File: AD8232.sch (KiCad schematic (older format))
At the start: 33 parts

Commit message: conectar simbolos en el esquematico
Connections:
- net GND: now reaches JP?.1 (A)
- net GND: now also C?.1, C?.1, J?.1 (Pin_1), M?.16 (GND), M?.PAD (GND_PAD), R?.1, R?.2
- net at JP?.2 (B): now also D?.1 (K)
- net RL: now reaches J?.1 (Pin_1)
- net RL: now also J?.T, R?.2
- net LA: now reaches J?.2 (Pin_2)
- net LA: now also J?.R, R?.2, R?.2
- net RA: now reaches J?.3 (Pin_3)
- net RA: now also J?.S, R?.2, R?.2
- net at D?.2 (A): now also R?.2
- net +3V3: now reaches J?.2 (Pin_2)
- net +3V3: now also C?.2, M?.15 (FR), M?.17 (+VS), R?.1, R?.1, R?.2, R?.2
- net SIGNAL_OUT: now reaches J?.3 (Pin_3)
- net SIGNAL_OUT: now also C?.2, M?.10 (OUT), R?.1, R?.2
- net LO-: now reaches J?.4 (Pin_4)
- net LO-: now also M?.11 (LO-)
- net LO+: now reaches J?.5 (Pin_5)
- net LO+: now also M?.12 (LO+)
- net SDN: now reaches J?.6 (Pin_6)
- net SDN: now also M?.13 (~SDN), R?.2
- net at M?.1 (HPDRIVE): now also C?.2
- net at M?.14 (AC/~DC): now also R?.1, R?.2
- net at M?.18 (REFIN): now also C?.2, R?.1, R?.2
- net at M?.19 (IAOUT): now also R?.1, R?.1
- net at M?.2 (+IN): now also R?.1
- net at M?.20 (HPSENSE): now also C?.1, R?.2
- net at M?.3 (-IN): now also R?.1
- net at M?.4 (RLDFB): now also C?.1
- net at M?.5 (RLD): now also C?.2, R?.1
- net at M?.6 (SW): now also C?.2, R?.1, R?.2
- net at M?.7 (OPAMP+): now also C?.1, R?.1
- net REFOUT: now reaches M?.8 (REFOUT)
- net REFOUT: now also C?.1, C?.2, R?.1
- net at M?.9 (OPAMP-): now also R?.1, R?.2
- net at R?.1: now also R?.1, R?.1, R?.2
- net at R?.2: now also C?.1, R?.2
- net at R?.1: now also R?.1, R?.2
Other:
- moved on the sheet: C?, D?, J?, JP?, M?, R?

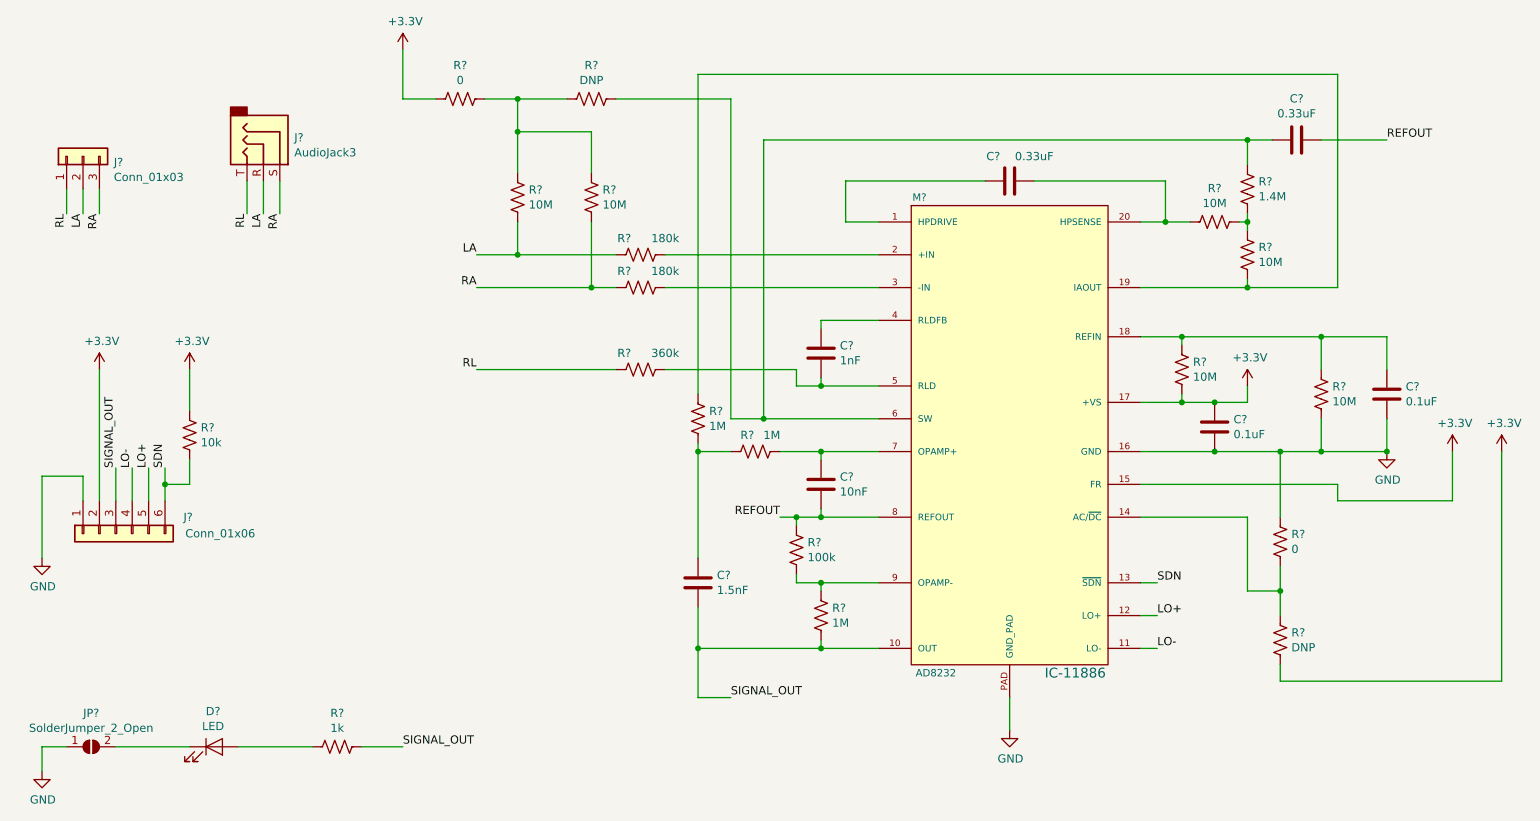
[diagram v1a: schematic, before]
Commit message: anotar simbolos del esquema
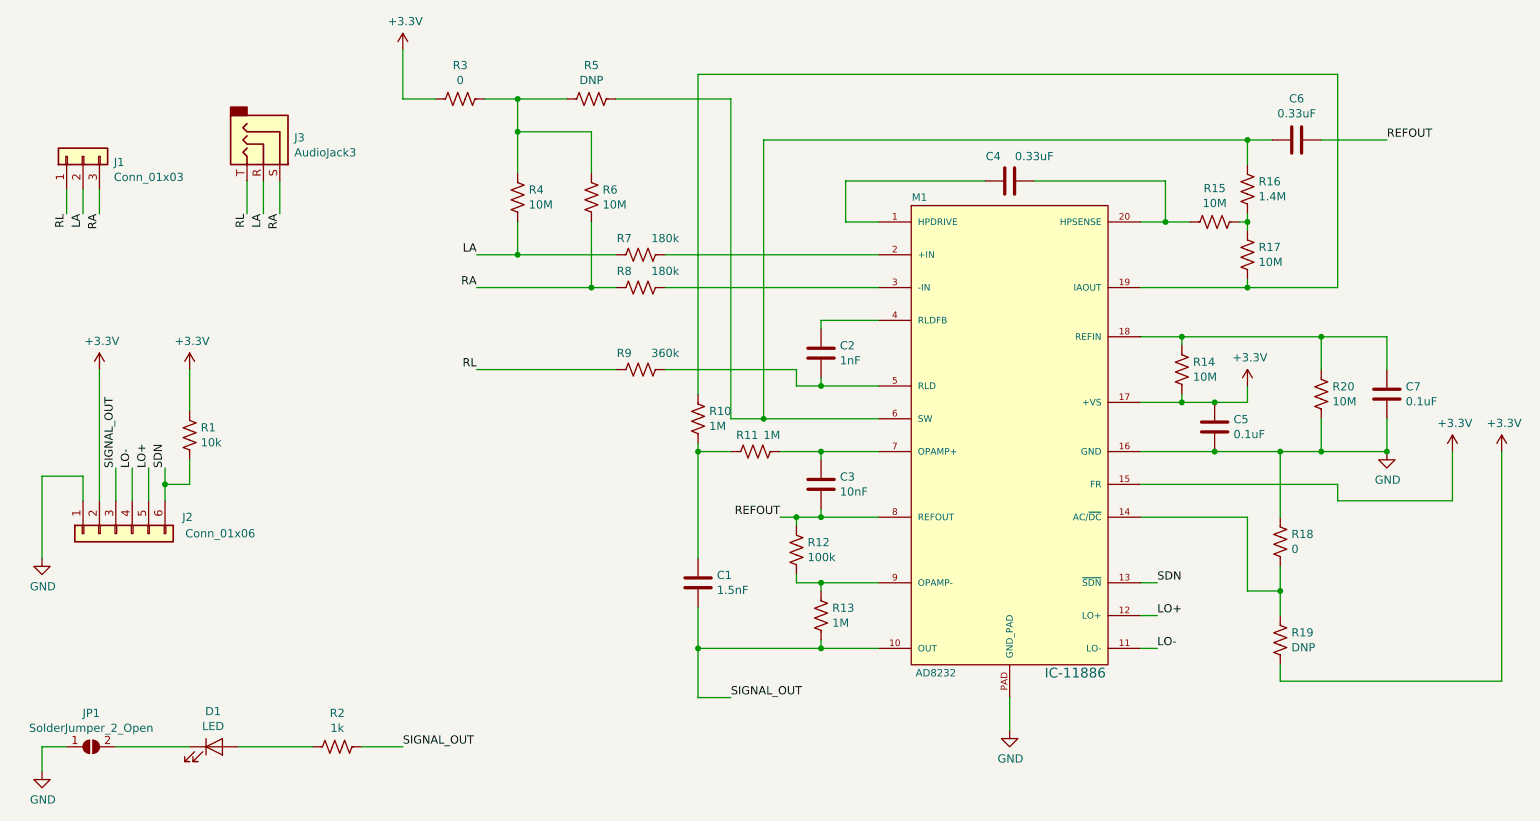
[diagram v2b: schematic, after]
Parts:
- gave numbers to parts that had none: 33

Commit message: agregar huellas a los simbolos en el esquematico
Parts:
- C1, C2, C3, C5, C7: footprint (none) -> Capacitor_SMD:C_0603_1608Metric
- C4, C6: footprint (none) -> Capacitor_SMD:C_0805_2012Metric
- D1: footprint (none) -> LED_SMD:LED_0603_1608Metric
- J1: footprint (none) -> Connector_Wire:SolderWirePad_1x03_P7.62mm_Drill2.5mm
- J2: footprint (none) -> TerminalBlock_TE-Connectivity:TerminalBlock_TE_282834-6_1x06_P2.54mm_Horizontal
- J3: footprint (none) -> Connector_Audio:Jack_3.5mm_CUI_SJ-3523-SMT_Horizontal
- JP1: footprint (none) -> Jumper:SolderJumper-2_P1.3mm_Open_RoundedPad1.0x1.5mm
- M1: footprint LFCSP_20 -> Package_CSP:LFCSP-20-1EP_4x4mm_P0.5mm_EP2.5x2.5mm
- R1, R10, R11, R12, R13, R14, R15, R16, R17, R18, R19, R2, R20, R3, R4, R5, R6, R7, R8, R9: footprint (none) -> Resistor_SMD:R_0603_1608Metric
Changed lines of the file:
@@
 F 0 "J1" V 1664 2212 50  0000 R CNN
 F 1 "Conn_01x03" V 1573 2212 50  0000 R CNN
-F 2 "" H 1700 2400 50  0001 C CNN
+F 2 "Connector_Wire:SolderWirePad_1x03_P7.62mm_Drill2.5mm" H 1700 2400 50  0001 C CNN
 F 3 "~" H 1700 2400 50  0001 C CNN
 	1    1700 2400
@@
 F 0 "J3" V 2736 2538 50  0000 L CNN
 F 1 "AudioJack3" V 2827 2538 50  0000 L CNN
-F 2 "" H 2800 2350 50  0001 C CNN
+F 2 "Connector_Audio:Jack_3.5mm_CUI_SJ-3523-SMT_Horizontal" H 2800 2350 50  0001 C CNN
 F 3 "~" H 2800 2350 50  0001 C CNN
 	1    2800 2350
@@
 F 0 "JP1" H 1750 6205 50  0000 C CNN
 F 1 "SolderJumper_2_Open" H 1750 6114 50  0000 C CNN
-F 2 "" H 1750 6000 50  0001 C CNN
+F 2 "Jumper:SolderJumper-2_P1.3mm_Open_RoundedPad1.0x1.5mm" H 1750 6000 50  0001 C CNN
 F 3 "~" H 1750 6000 50  0001 C CNN
 	1    1750 6000
@@
 F 0 "D1" H 2493 6216 50  0000 C CNN
 F 1 "LED" H 2493 6125 50  0000 C CNN
-F 2 "" H 2500 6000 50  0001 C CNN
+F 2 "LED_SMD:LED_0603_1608Metric" H 2500 6000 50  0001 C CNN
 F 3 "~" H 2500 6000 50  0001 C CNN
 	1    2500 6000
@@
 F 0 "R4" H 4418 2696 50  0000 L CNN
 F 1 "10M" H 4418 2605 50  0000 L CNN
-F 2 "" V 4390 2640 50  0001 C CNN
+F 2 "Resistor_SMD:R_0603_1608Metric" V 4390 2640 50  0001 C CNN
 F 3 "~" H 4350 2650 50  0001 C CNN
 	1    4350 2650
@@
 F 0 "R6" H 4868 2696 50  0000 L CNN
 F 1 "10M" H 4868 2605 50  0000 L CNN
-F 2 "" V 4840 2640 50  0001 C CNN
+F 2 "Resistor_SMD:R_0603_1608Metric" V 4840 2640 50  0001 C CNN
 F 3 "~" H 4800 2650 50  0001 C CNN
 	1    4800 2650
@@
 F 0 "R7" V 5000 2900 50  0000 C CNN
 F 1 "180k" V 5000 3150 50  0000 C CNN
-F 2 "" V 5140 2990 50  0001 C CNN
+F 2 "Resistor_SMD:R_0603_1608Metric" V 5140 2990 50  0001 C CNN
 F 3 "~" H 5100 3000 50  0001 C CNN
 	1    5100 3000
@@
 F 0 "R8" V 5000 3100 50  0000 C CNN
 F 1 "180k" V 5000 3350 50  0000 C CNN
-F 2 "" V 5140 3190 50  0001 C CNN
+F 2 "Resistor_SMD:R_0603_1608Metric" V 5140 3190 50  0001 C CNN
 F 3 "~" H 5100 3200 50  0001 C CNN
 	1    5100 3200
@@
 F 0 "R9" V 5000 3600 50  0000 C CNN
 F 1 "360k" V 5000 3850 50  0000 C CNN
-F 2 "" V 5140 3690 50  0001 C CNN
+F 2 "Resistor_SMD:R_0603_1608Metric" V 5140 3690 50  0001 C CNN
 F 3 "~" H 5100 3700 50  0001 C CNN
 	1    5100 3700
@@
 F 0 "R10" H 5518 4046 50  0000 L CNN
 F 1 "1M" H 5518 3955 50  0000 L CNN
-F 2 "" V 5490 3990 50  0001 C CNN
+F 2 "Resistor_SMD:R_0603_1608Metric" V 5490 3990 50  0001 C CNN
 F 3 "~" H 5450 4000 50  0001 C CNN
 	1    5450 4000
@@
 F 0 "R11" V 5700 4150 50  0000 C CNN
 F 1 "1M" V 5700 4300 50  0000 C CNN
-F 2 "" V 5840 4190 50  0001 C CNN
+F 2 "Resistor_SMD:R_0603_1608Metric" V 5840 4190 50  0001 C CNN
 F 3 "~" H 5800 4200 50  0001 C CNN
 	1    5800 4200
@@
 F 0 "C1" H 5565 5046 50  0000 L CNN
 F 1 "1.5nF" H 5565 4955 50  0000 L CNN
-F 2 "" H 5488 4850 50  0001 C CNN
+F 2 "Capacitor_SMD:C_0603_1608Metric" H 5488 4850 50  0001 C CNN
 F 3 "~" H 5450 5000 50  0001 C CNN
 	1    5450 5000
@@
 F 0 "C2" H 6315 3646 50  0000 L CNN
 F 1 "1nF" H 6315 3555 50  0000 L CNN
-F 2 "" H 6238 3450 50  0001 C CNN
+F 2 "Capacitor_SMD:C_0603_1608Metric" H 6238 3450 50  0001 C CNN
 F 3 "~" H 6200 3600 50  0001 C CNN
 	1    6200 3600
@@
 F 0 "C3" H 6315 4446 50  0000 L CNN
 F 1 "10nF" H 6315 4355 50  0000 L CNN
-F 2 "" H 6238 4250 50  0001 C CNN
+F 2 "Capacitor_SMD:C_0603_1608Metric" H 6238 4250 50  0001 C CNN
 F 3 "~" H 6200 4400 50  0001 C CNN
 	1    6200 4400
@@
 F 0 "R12" H 6118 4846 50  0000 L CNN
 F 1 "100k" H 6118 4755 50  0000 L CNN
-F 2 "" V 6090 4790 50  0001 C CNN
+F 2 "Resistor_SMD:R_0603_1608Metric" V 6090 4790 50  0001 C CNN
 F 3 "~" H 6050 4800 50  0001 C CNN
 	1    6050 4800
@@
 F 0 "R13" H 6268 5246 50  0000 L CNN
 F 1 "1M" H 6268 5155 50  0000 L CNN
-F 2 "" V 6240 5190 50  0001 C CNN
+F 2 "Resistor_SMD:R_0603_1608Metric" V 6240 5190 50  0001 C CNN
 F 3 "~" H 6200 5200 50  0001 C CNN
 	1    6200 5200
@@
 F 0 "C4" V 7200 2450 50  0000 C CNN
 F 1 "0.33uF" V 7200 2700 50  0000 C CNN
-F 2 "" H 7388 2400 50  0001 C CNN
+F 2 "Capacitor_SMD:C_0805_2012Metric" H 7388 2400 50  0001 C CNN
 F 3 "~" H 7350 2550 50  0001 C CNN
 	1    7350 2550
@@
 F 0 "M1" H 6800 6150 45  0000 C CNN
 F 1 "AD8232" H 6900 3250 45  0000 C CNN
-F 2 "LFCSP_20" H 7350 6200 20  0001 C CNN
+F 2 "Package_CSP:LFCSP-20-1EP_4x4mm_P0.5mm_EP2.5x2.5mm" H 7350 6200 20  0001 C CNN
 F 3 "" H 7350 4400 60  0001 C CNN
 F 4 "IC-11886" H 7750 3250 60  0000 C CNN "Campo4"
@@
 F 0 "C5" H 8485 4004 50  0000 R CNN
 F 1 "0.1uF" H 8485 4095 50  0000 R CNN
-F 2 "" H 8638 3900 50  0001 C CNN
+F 2 "Capacitor_SMD:C_0603_1608Metric" H 8638 3900 50  0001 C CNN
 F 3 "~" H 8600 4050 50  0001 C CNN
 	1    8600 4050
@@
 F 0 "R14" H 8468 3746 50  0000 L CNN
 F 1 "10M" H 8468 3655 50  0000 L CNN
-F 2 "" V 8440 3690 50  0001 C CNN
+F 2 "Resistor_SMD:R_0603_1608Metric" V 8440 3690 50  0001 C CNN
 F 3 "~" H 8400 3700 50  0001 C CNN
 	1    8400 3700
@@
 F 0 "R15" V 8395 2800 50  0000 C CNN
 F 1 "10M" V 8486 2800 50  0000 C CNN
-F 2 "" V 8640 2790 50  0001 C CNN
+F 2 "Resistor_SMD:R_0603_1608Metric" V 8640 2790 50  0001 C CNN
 F 3 "~" H 8600 2800 50  0001 C CNN
 	1    8600 2800
@@
 F 0 "R16" H 8732 2554 50  0000 R CNN
 F 1 "1.4M" H 8732 2645 50  0000 R CNN
-F 2 "" V 8840 2590 50  0001 C CNN
+F 2 "Resistor_SMD:R_0603_1608Metric" V 8840 2590 50  0001 C CNN
 F 3 "~" H 8800 2600 50  0001 C CNN
 	1    8800 2600
@@
 F 0 "R17" H 8732 2954 50  0000 R CNN
 F 1 "10M" H 8732 3045 50  0000 R CNN
-F 2 "" V 8840 2990 50  0001 C CNN
+F 2 "Resistor_SMD:R_0603_1608Metric" V 8840 2990 50  0001 C CNN
 F 3 "~" H 8800 3000 50  0001 C CNN
 	1    8800 3000
@@
 F 0 "C6" V 8848 2300 50  0000 C CNN
 F 1 "0.33uF" V 8939 2300 50  0000 C CNN
-F 2 "" H 9138 2150 50  0001 C CNN
+F 2 "Capacitor_SMD:C_0805_2012Metric" H 9138 2150 50  0001 C CNN
 F 3 "~" H 9100 2300 50  0001 C CNN
 	1    9100 2300
@@
 F 0 "R20" H 9182 3804 50  0000 R CNN
 F 1 "10M" H 9182 3895 50  0000 R CNN
-F 2 "" V 9290 3840 50  0001 C CNN
+F 2 "Resistor_SMD:R_0603_1608Metric" V 9290 3840 50  0001 C CNN
 F 3 "~" H 9250 3850 50  0001 C CNN
 	1    9250 3850
@@
 F 0 "C7" H 9535 3804 50  0000 R CNN
 F 1 "0.1uF" H 9535 3895 50  0000 R CNN
-F 2 "" H 9688 3700 50  0001 C CNN
+F 2 "Capacitor_SMD:C_0603_1608Metric" H 9688 3700 50  0001 C CNN
 F 3 "~" H 9650 3850 50  0001 C CNN
 	1    9650 3850
@@
 F 0 "R1" H 2418 4146 50  0000 L CNN
 F 1 "10k" H 2418 4055 50  0000 L CNN
-F 2 "" V 2390 4090 50  0001 C CNN
+F 2 "Resistor_SMD:R_0603_1608Metric" V 2390 4090 50  0001 C CNN
 F 3 "~" H 2350 4100 50  0001 C CNN
 	1    2350 4100
@@
 F 0 "R2" V 3045 6000 50  0000 C CNN
 F 1 "1k" V 3136 6000 50  0000 C CNN
-F 2 "" V 3290 5990 50  0001 C CNN
+F 2 "Resistor_SMD:R_0603_1608Metric" V 3290 5990 50  0001 C CNN
 F 3 "~" H 3250 6000 50  0001 C CNN
 	1    3250 6000
@@
 F 0 "R3" V 3795 2050 50  0000 C CNN
 F 1 "0" V 3886 2050 50  0000 C CNN
-F 2 "" V 4040 2040 50  0001 C CNN
+F 2 "Resistor_SMD:R_0603_1608Metric" V 4040 2040 50  0001 C CNN
 F 3 "~" H 4000 2050 50  0001 C CNN
 	1    4000 2050
@@
 F 0 "R5" V 4595 2050 50  0000 C CNN
 F 1 "DNP" V 4686 2050 50  0000 C CNN
-F 2 "" V 4840 2040 50  0001 C CNN
+F 2 "Resistor_SMD:R_0603_1608Metric" V 4840 2040 50  0001 C CNN
 F 3 "~" H 4800 2050 50  0001 C CNN
 	1    4800 2050
@@
 F 0 "R18" H 8932 4704 50  0000 R CNN
 F 1 "0" H 8932 4795 50  0000 R CNN
-F 2 "" V 9040 4740 50  0001 C CNN
+F 2 "Resistor_SMD:R_0603_1608Metric" V 9040 4740 50  0001 C CNN
 F 3 "~" H 9000 4750 50  0001 C CNN
 	1    9000 4750
@@
 F 0 "R19" H 8932 5304 50  0000 R CNN
 F 1 "DNP" H 8932 5395 50  0000 R CNN
-F 2 "" V 9040 5340 50  0001 C CNN
+F 2 "Resistor_SMD:R_0603_1608Metric" V 9040 5340 50  0001 C CNN
 F 3 "~" H 9000 5350 50  0001 C CNN
 	1    9000 5350
@@
 F 0 "J2" V 1800 4231 50  0000 L CNN
 F 1 "Conn_01x06" V 1900 3850 50  0000 L CNN
-F 2 "" H 1900 4700 50  0001 C CNN
+F 2 "TerminalBlock_TE-Connectivity:TerminalBlock_TE_282834-6_1x06_P2.54mm_Horizontal" H 1900 4700 50  0001 C CNN
 F 3 "~" H 1900 4700 50  0001 C CNN
 	1    1900 4700

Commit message: agregar huella de SparkFun para LFCSP_20 y usar en AD8232
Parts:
- M1: footprint Package_CSP:LFCSP-20-1EP_4x4mm_P0.5mm_EP2.5x2.5mm -> fp:LFCSP_20
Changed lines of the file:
@@
 F 0 "M1" H 6800 6150 45  0000 C CNN
 F 1 "AD8232" H 6900 3250 45  0000 C CNN
-F 2 "Package_CSP:LFCSP-20-1EP_4x4mm_P0.5mm_EP2.5x2.5mm" H 7350 6200 20  0001 C CNN
+F 2 "fp:LFCSP_20" H 7350 6200 20  0001 C CNN
 F 3 "" H 7350 4400 60  0001 C CNN
 F 4 "IC-11886" H 7750 3250 60  0000 C CNN "Campo4"

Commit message: usar huellas de conectores 1x03 y 1x06 de SparkFun
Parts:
- J1: footprint Connector_Wire:SolderWirePad_1x03_P7.62mm_Drill2.5mm -> fp:1X03
- J2: footprint TerminalBlock_TE-Connectivity:TerminalBlock_TE_282834-6_1x06_P2.54mm_Horizontal -> fp:1X06
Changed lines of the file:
@@
 F 0 "J1" V 1664 2212 50  0000 R CNN
 F 1 "Conn_01x03" V 1573 2212 50  0000 R CNN
-F 2 "Connector_Wire:SolderWirePad_1x03_P7.62mm_Drill2.5mm" H 1700 2400 50  0001 C CNN
+F 2 "fp:1X03" H 1700 2400 50  0001 C CNN
 F 3 "~" H 1700 2400 50  0001 C CNN
 	1    1700 2400
@@
 F 0 "J2" V 1800 4231 50  0000 L CNN
 F 1 "Conn_01x06" V 1900 3850 50  0000 L CNN
-F 2 "TerminalBlock_TE-Connectivity:TerminalBlock_TE_282834-6_1x06_P2.54mm_Horizontal" H 1900 4700 50  0001 C CNN
+F 2 "fp:1X06" H 1900 4700 50  0001 C CNN
 F 3 "~" H 1900 4700 50  0001 C CNN
 	1    1900 4700
